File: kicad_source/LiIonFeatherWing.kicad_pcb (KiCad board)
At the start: 2 copper layers, 80 x 48 mm, 5 parts, among them CN1 ADAFRUIT_FEATHER, CN2 CONN_01X04, CN3 CONN_01X04, SW1 SWITCH_INV

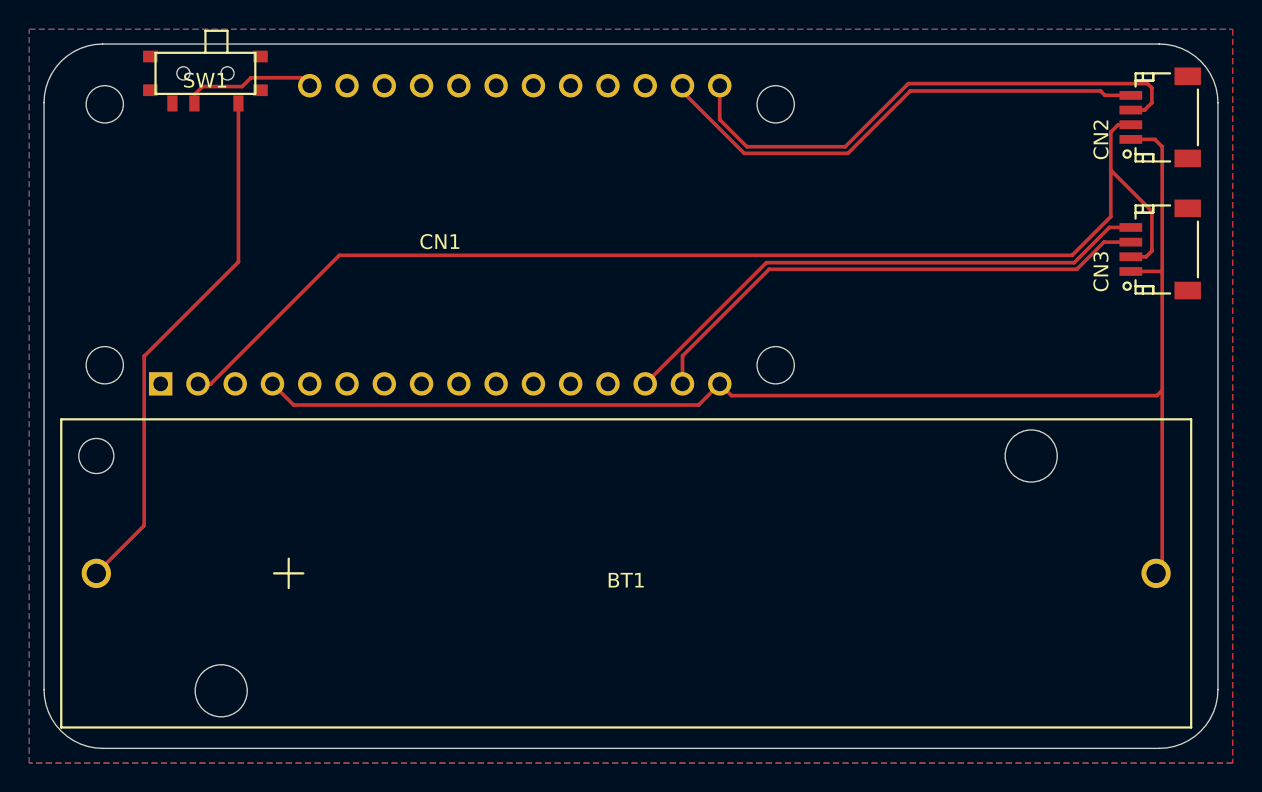
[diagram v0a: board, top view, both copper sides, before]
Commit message: added mounting holes and labels
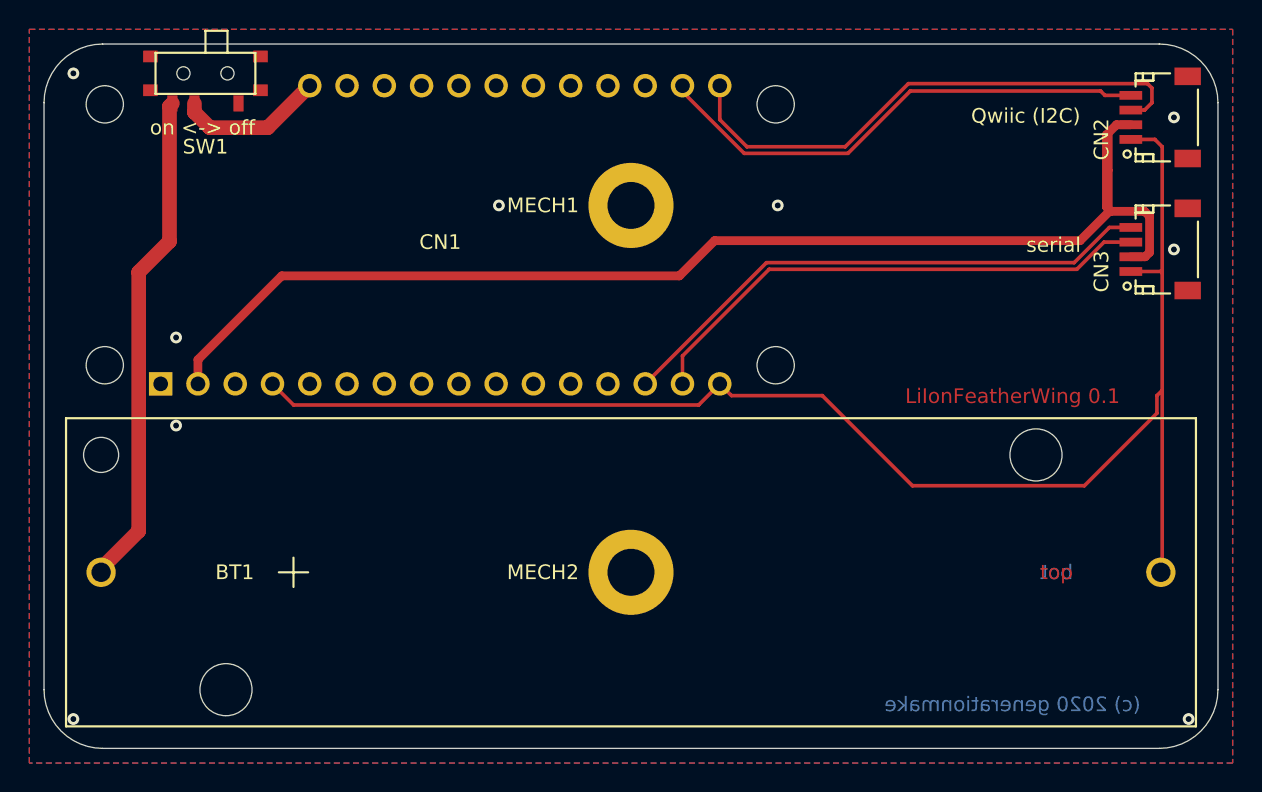
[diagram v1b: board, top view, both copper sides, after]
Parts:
- added L1: Label, labels:generationmake_small_solder, F.Cu at (171.7, 108.8)
- added L2: Label, labels:generationmake_logo, B.Cu at (170.0, 112.0)
- added MECH1: MHP_3.2_5.8, MECH_mounting_holes:MHP_3.2_5.8, F.Cu at (144.0, 96.0)
- added MECH2: MHP_3.2_5.8, MECH_mounting_holes:MHP_3.2_5.8, F.Cu at (144.0, 121.0)
- moved BT1 0.33 mm to (144.0, 121.0)
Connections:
- SW1 pad 1: +BATT -> (no net)
- SW1 pad 3: (no net) -> +BATT
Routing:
- net +3V3: track 82.5 -> 88.9 mm
- net GND: track 96.1 -> 101.9 mm, vias 0 -> 9
- net +BATT: track 36.0 -> 34.2 mm
- net /VBAT: track 9.16 -> 10.1 mm
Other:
- board text added: "(c) 2020 generationmake"
- board text added: "LiIonFeatherWing"
- board text added: "LiIonFeatherWing 0.1"
- board text added: "Qwiic (I2C)"
- board text added: "bot"
- board text added: "on <-> off"
- board text added: "serial"
- board text added: "top"

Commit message: added testpoints and array
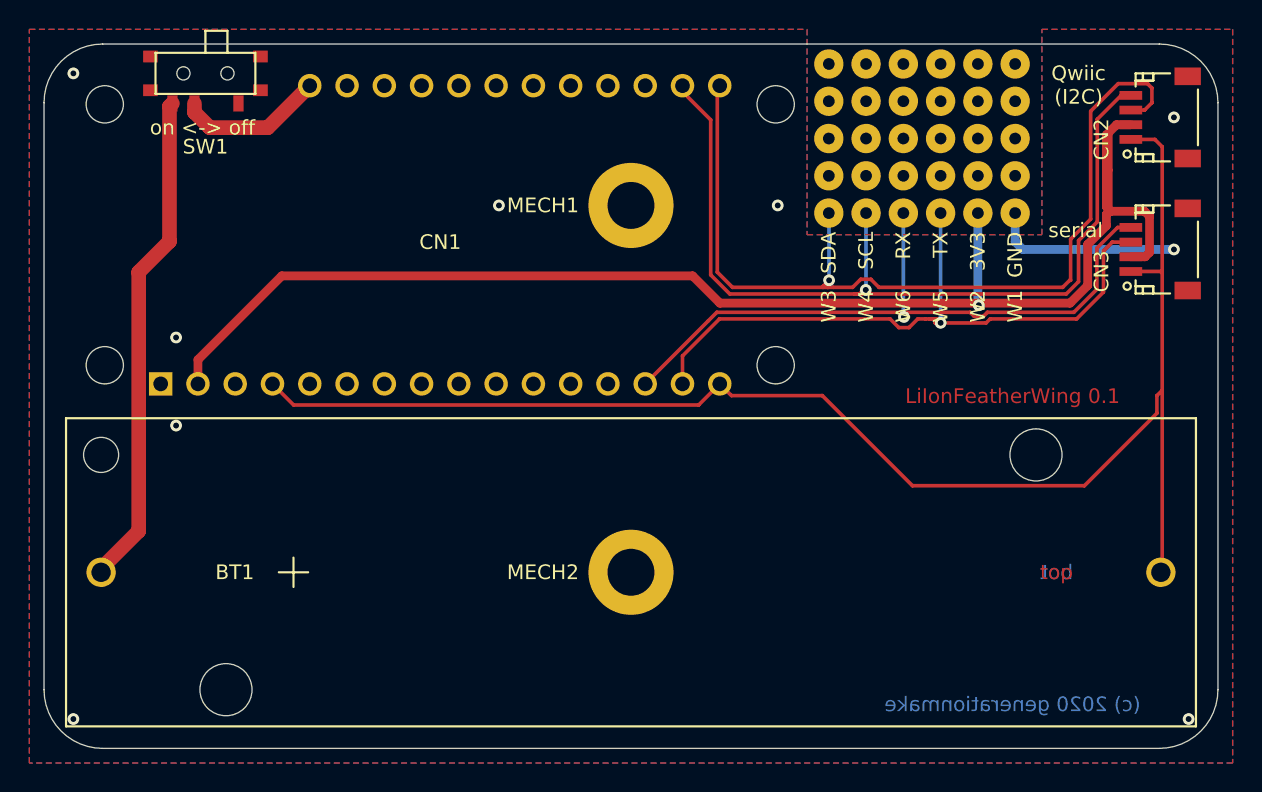
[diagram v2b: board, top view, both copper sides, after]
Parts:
- added REF**: SolderWirePad_single_0-8mmDrill, wire_pads:SolderWirePad_single_0-8mmDrill, F.Cu at (157.5, 94.0)
- added REF**: SolderWirePad_single_0-8mmDrill, wire_pads:SolderWirePad_single_0-8mmDrill, F.Cu at (162.6, 91.4)
- added REF**: SolderWirePad_single_0-8mmDrill, wire_pads:SolderWirePad_single_0-8mmDrill, F.Cu at (165.1, 91.4)
- added REF**: SolderWirePad_single_0-8mmDrill, wire_pads:SolderWirePad_single_0-8mmDrill, F.Cu at (160.0, 91.4)
- added REF**: SolderWirePad_single_0-8mmDrill, wire_pads:SolderWirePad_single_0-8mmDrill, F.Cu at (157.5, 86.4)
- added REF**: SolderWirePad_single_0-8mmDrill, wire_pads:SolderWirePad_single_0-8mmDrill, F.Cu at (162.6, 86.4)
- added REF**: SolderWirePad_single_0-8mmDrill, wire_pads:SolderWirePad_single_0-8mmDrill, F.Cu at (167.6, 86.4)
- added REF**: SolderWirePad_single_0-8mmDrill, wire_pads:SolderWirePad_single_0-8mmDrill, F.Cu at (160.0, 86.4)
- added REF**: SolderWirePad_single_0-8mmDrill, wire_pads:SolderWirePad_single_0-8mmDrill, F.Cu at (165.1, 86.4)
- added REF**: SolderWirePad_single_0-8mmDrill, wire_pads:SolderWirePad_single_0-8mmDrill, F.Cu at (170.2, 86.4)
- added REF**: SolderWirePad_single_0-8mmDrill, wire_pads:SolderWirePad_single_0-8mmDrill, F.Cu at (170.2, 88.9)
- added REF**: SolderWirePad_single_0-8mmDrill, wire_pads:SolderWirePad_single_0-8mmDrill, F.Cu at (165.1, 94.0)
- added REF**: SolderWirePad_single_0-8mmDrill, wire_pads:SolderWirePad_single_0-8mmDrill, F.Cu at (167.6, 88.9)
- added REF**: SolderWirePad_single_0-8mmDrill, wire_pads:SolderWirePad_single_0-8mmDrill, F.Cu at (165.1, 88.9)
- added REF**: SolderWirePad_single_0-8mmDrill, wire_pads:SolderWirePad_single_0-8mmDrill, F.Cu at (162.6, 88.9)
- added REF**: SolderWirePad_single_0-8mmDrill, wire_pads:SolderWirePad_single_0-8mmDrill, F.Cu at (160.0, 88.9)
- added REF**: SolderWirePad_single_0-8mmDrill, wire_pads:SolderWirePad_single_0-8mmDrill, F.Cu at (157.5, 88.9)
- added REF**: SolderWirePad_single_0-8mmDrill, wire_pads:SolderWirePad_single_0-8mmDrill, F.Cu at (162.6, 94.0)
- added REF**: SolderWirePad_single_0-8mmDrill, wire_pads:SolderWirePad_single_0-8mmDrill, F.Cu at (160.0, 94.0)
- added REF**: SolderWirePad_single_0-8mmDrill, wire_pads:SolderWirePad_single_0-8mmDrill, F.Cu at (170.2, 94.0)
- added REF**: SolderWirePad_single_0-8mmDrill, wire_pads:SolderWirePad_single_0-8mmDrill, F.Cu at (167.6, 94.0)
- added REF**: SolderWirePad_single_0-8mmDrill, wire_pads:SolderWirePad_single_0-8mmDrill, F.Cu at (170.2, 91.4)
- added REF**: SolderWirePad_single_0-8mmDrill, wire_pads:SolderWirePad_single_0-8mmDrill, F.Cu at (157.5, 91.4)
- added REF**: SolderWirePad_single_0-8mmDrill, wire_pads:SolderWirePad_single_0-8mmDrill, F.Cu at (167.6, 91.4)
- added W1: TEST_1P, wire_pads:SolderWirePad_single_0-8mmDrill, F.Cu at (170.2, 96.5)
- added W2: TEST_1P, wire_pads:SolderWirePad_single_0-8mmDrill, F.Cu at (167.6, 96.5)
- added W3: TEST_1P, wire_pads:SolderWirePad_single_0-8mmDrill, F.Cu at (157.5, 96.5)
- added W4: TEST_1P, wire_pads:SolderWirePad_single_0-8mmDrill, F.Cu at (160.0, 96.5)
- added W5: TEST_1P, wire_pads:SolderWirePad_single_0-8mmDrill, F.Cu at (165.1, 96.5)
- added W6: TEST_1P, wire_pads:SolderWirePad_single_0-8mmDrill, F.Cu at (162.6, 96.5)
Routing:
- net /I2C_SDA: track 37.1 -> 63.5 mm, vias 0 -> 1
- net /I2C_SCL: track 34.6 -> 60.2 mm, vias 0 -> 1
- net GND: track 101.9 -> 114.9 mm
- net /SERIAL_TX: track 35.7 -> 46.7 mm, vias 0 -> 1
- net +3V3: track 88.9 -> 99.1 mm, vias 0 -> 1
- net /SERIAL_RX: track 37.5 -> 47.0 mm, vias 0 -> 1
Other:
- board text added: "3V3"
- board text added: "GND"
- board text added: "RX"
- board text added: "SCL"
- board text added: "SDA"
- board text added: "TX"
